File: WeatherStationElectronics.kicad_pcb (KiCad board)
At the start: 2 copper layers, 4 parts, among them U1 ESP32-WROOM-32D, U2 L78L33_TO92, U3 DHT11, U4 BMP280

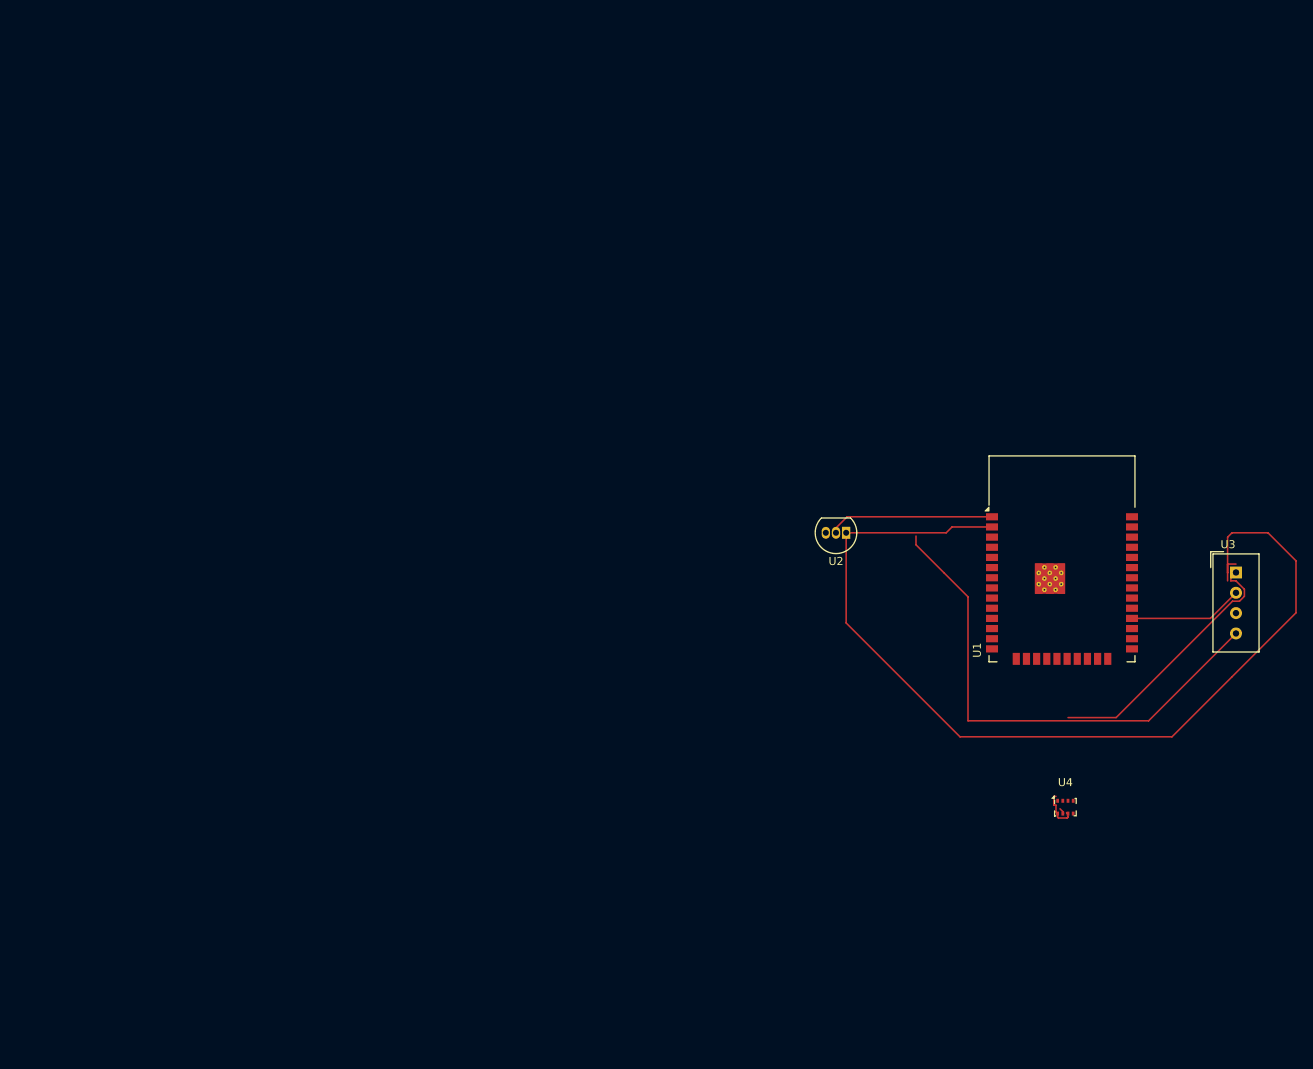
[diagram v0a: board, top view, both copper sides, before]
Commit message: first PCB
todo: add a power switch
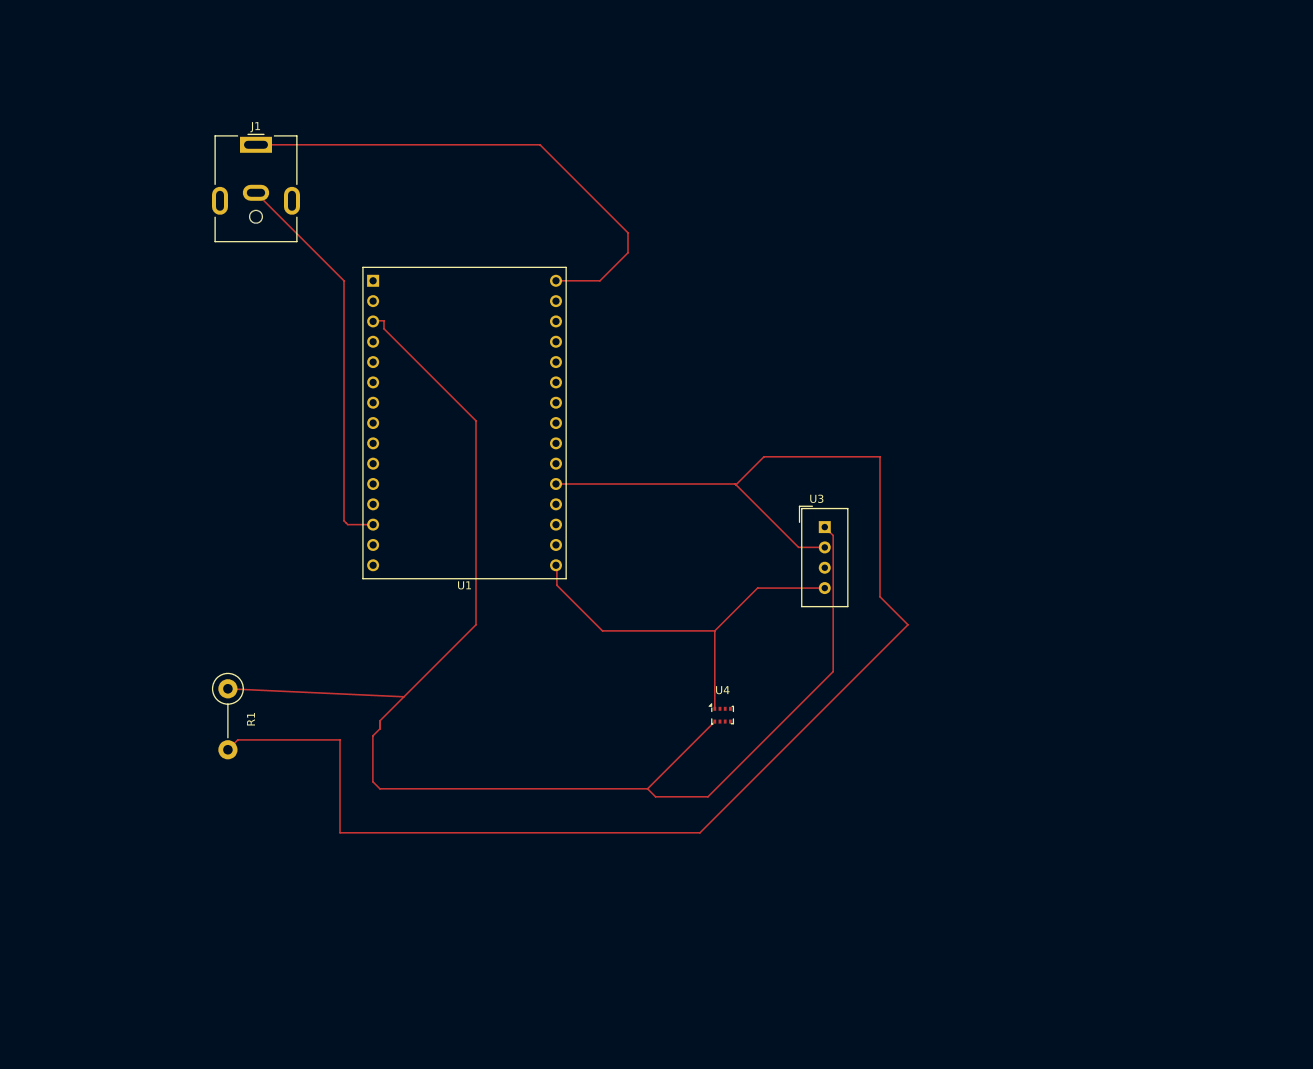
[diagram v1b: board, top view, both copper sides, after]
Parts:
- removed U2: L78L33_TO92, Package_TO_SOT_THT:TO-92_Inline
- added J1: Barrel_Jack, Connector_BarrelJack:BarrelJack_CUI_PJ-063AH_Horizontal, F.Cu at (60.0, 31.0)
- added R1: 5kOhm, Resistor_THT:R_Axial_DIN0411_L9.9mm_D3.6mm_P7.62mm_Vertical, F.Cu at (56.5, 99.0)
- U1: value ESP32-WROOM-32D -> ESP32-C3-DevKitM-1; footprint RF_Module:ESP32-WROOM-32D -> RF_Module:ESP32-C3-DevKitM-1
- moved U1 94.0 mm to (74.6, 48.0)
- moved U3 51.7 mm to (131.1, 78.8)
- moved U4 44.4 mm to (118.3, 102.3)
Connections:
- net +3V3 renamed +3.3V
- U1 pad 1: Net-(U2-GND) -> GND
- U1 pad 10: Net-(U1-IO25) -> unconnected-(U1-IO1-Pad10)
- U1 pad 11: Net-(U1-IO26) -> unconnected-(U1-IO10-Pad11)
- U1 pad 12: unconnected-(U1-IO27-Pad12) -> GND
- U1 pad 13: unconnected-(U1-IO14-Pad13) -> +5V
- U1 pad 14: unconnected-(U1-IO12-Pad14) -> +5V
- U1 pad 15: Net-(U2-GND) -> GND
- U1 pad 16: unconnected-(U1-IO13-Pad16) -> GND
- U1 pad 19: unconnected-(U1-SCS/CMD-Pad19) -> GND
- U1 pad 2: Net-(U1-VDD) -> Net-(R1-Pad1)
- U1 pad 20: unconnected-(U1-SCK/CLK-Pad20) -> Net-(U1-IO4)
- U1 pad 24: unconnected-(U1-IO2-Pad24) -> GND
- U1 pad 25: unconnected-(U1-IO0-Pad25) -> Net-(U1-IO8)
- U1 pad 26: unconnected-(U1-IO4-Pad26) -> Net-(U1-IO9)
- U1 pad 27: unconnected-(U1-IO16-Pad27) -> GND
- U1 pad 28: Net-(U1-IO17) -> unconnected-(U1-RX-Pad28)
- U1 pad 3: unconnected-(U1-EN-Pad3) -> Net-(R1-Pad1)
- U1 pad 30: unconnected-(U1-IO18-Pad30) -> GND
- U1 pad 6: unconnected-(U1-IO34-Pad6) -> GND
- U1 pad 8: unconnected-(U1-IO32-Pad8) -> GND
- U3 pad 2: Net-(U1-IO17) -> Net-(U1-IO4)
- U4 pad 2: Net-(U1-IO26) -> unconnected-(U4-CSB-Pad2)
- U4 pad 3: Net-(U1-IO23) -> Net-(U1-IO8)
- U4 pad 4: Net-(U1-IO21) -> Net-(U1-IO9)
- U4 pad 5: Net-(U1-IO25) -> unconnected-(U4-SDO-Pad5)
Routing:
- net Net-(U1-IO4): track 0.00 -> 186.7 mm
- net +3.3V: track 38.2 -> 161.9 mm
- net Net-(U1-VDD): track 122.7 -> 0.00 mm
- net GND: track 64.7 -> 114.4 mm
- net +5V: track 0.00 -> 49.4 mm
- net Net-(U2-GND): track 20.7 -> 0.00 mm
- net Net-(U1-IO17): track 14.3 -> 0.00 mm

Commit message: update PCB and add a power switch
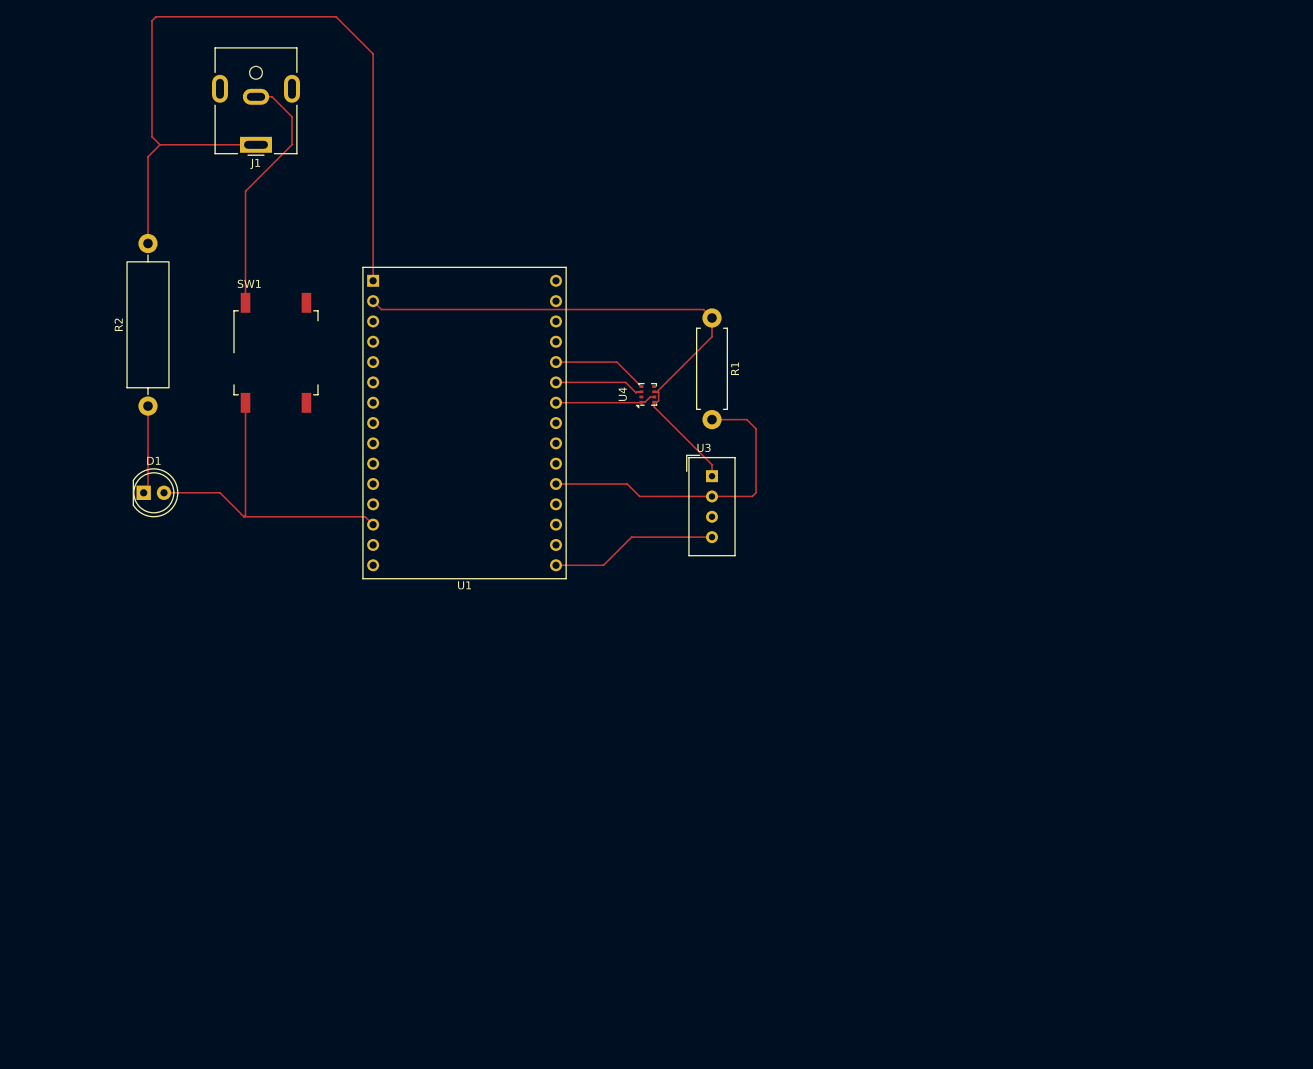
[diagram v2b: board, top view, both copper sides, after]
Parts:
- added D1: LED, LED_THT:LED_D5.0mm_Clear, F.Cu at (46.0, 74.5)
- added R2: 300 Ohm, Resistor_THT:R_Axial_DIN0516_L15.5mm_D5.0mm_P20.32mm_Horizontal, F.Cu at (46.5, 63.7)
- added SW1: SW_SPST, Button_Switch_SMD:SW_MEC_5GSH9, F.Cu at (62.5, 57.0)
- R1: footprint Resistor_THT:R_Axial_DIN0411_L9.9mm_D3.6mm_P7.62mm_Vertical -> Resistor_THT:R_Axial_DIN0411_L9.9mm_D3.6mm_P12.70mm_Horizontal
- moved R1 76.2 mm to (117.0, 52.6)
- moved U4 41.2 mm to (109.0, 62.2), turned to 90 degrees
- moved U3 15.5 mm to (117.0, 72.4)
- turned J1 to 180 degrees
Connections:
- J1 pad 2: +5V -> Net-(SW1-A)
- R1 pad 1: Net-(R1-Pad1) -> +3.3V
- U1 pad 2: Net-(R1-Pad1) -> +3.3V
- U1 pad 3: Net-(R1-Pad1) -> +3.3V
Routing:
- net Net-(U1-IO4): track 186.7 -> 39.8 mm
- net +3.3V: track 161.9 -> 70.1 mm
- net Net-(SW1-A): track 0.00 -> 31.2 mm
- net GND: track 114.4 -> 133.7 mm
- net Net-(U1-IO9): track 0.00 -> 11.9 mm
- net Net-(U1-IO8): track 0.00 -> 11.8 mm
- net Net-(D1-K): track 0.00 -> 11.1 mm
- net +5V: track 49.4 -> 42.1 mm

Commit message: define a pcb outline
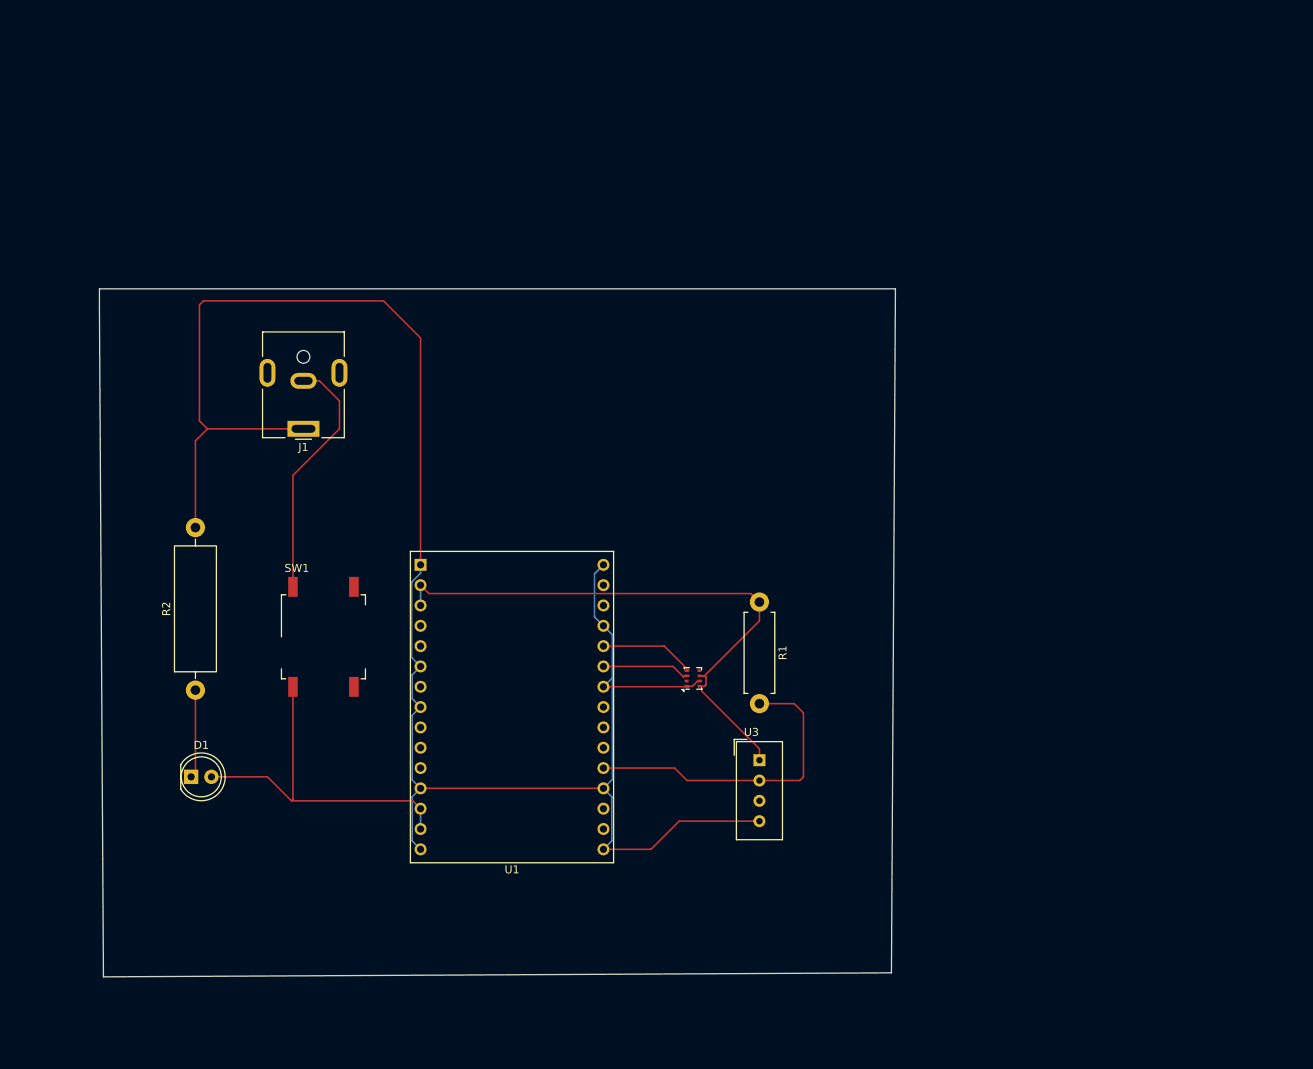
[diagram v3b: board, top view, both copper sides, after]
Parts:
- moved R2 36.0 mm to (52.4, 99.2)
- moved R1 36.0 mm to (122.9, 88.2)
- moved D1 36.0 mm to (51.9, 110.0)
- moved J1 36.0 mm to (65.9, 66.5)
- moved SW1 36.0 mm to (68.4, 92.5)
- moved U1 36.0 mm to (80.6, 83.5)
- moved U3 36.0 mm to (122.9, 107.9)
- moved U4 36.0 mm to (114.6, 97.7)
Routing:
- net GND: track 133.7 -> 235.5 mm
- net +3.3V: track 70.1 -> 72.7 mm
- net +5V: track 42.1 -> 44.7 mm
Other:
- board outline added: 99.5 x 86 mm
